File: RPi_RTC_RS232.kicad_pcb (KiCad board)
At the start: 2 copper layers, 65 x 56 mm, 5 parts, among them J2 RPi_GPIO

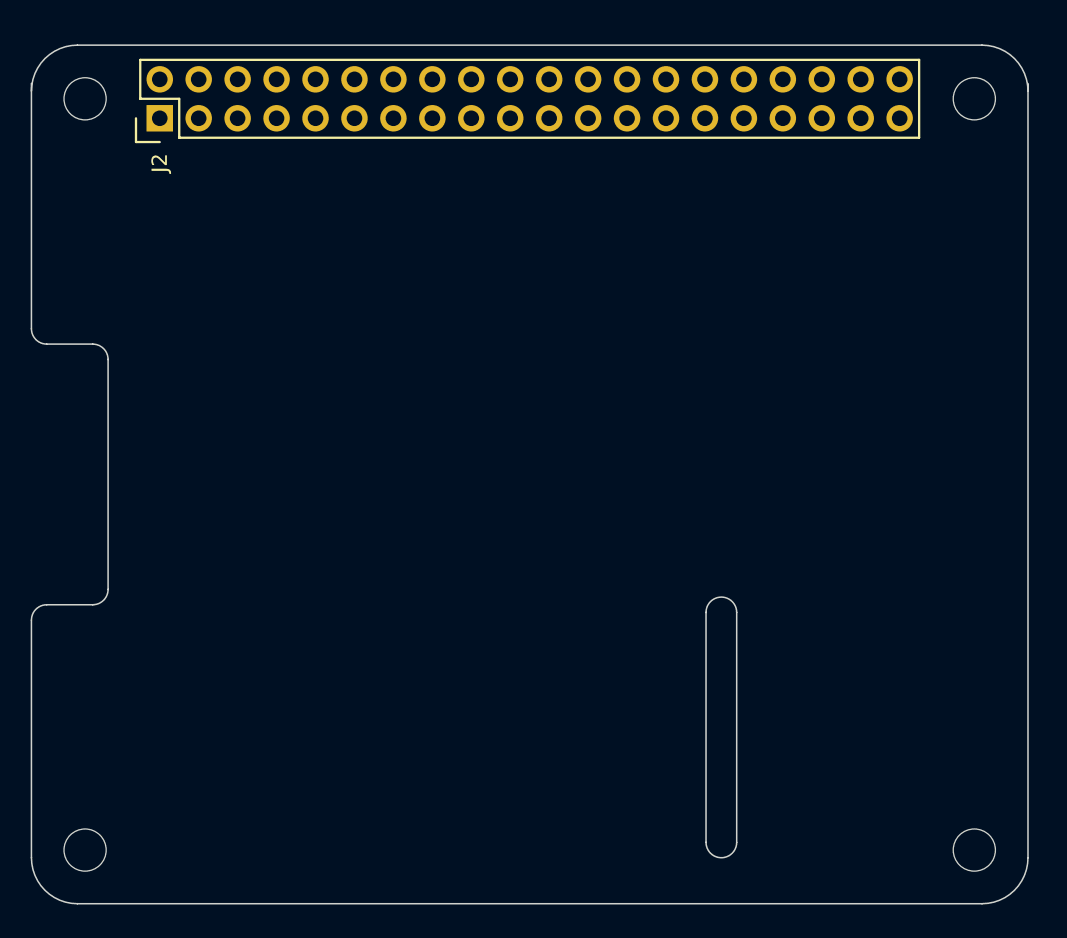
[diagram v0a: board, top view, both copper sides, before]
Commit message: schematic and provisional layout for RTC and RS232
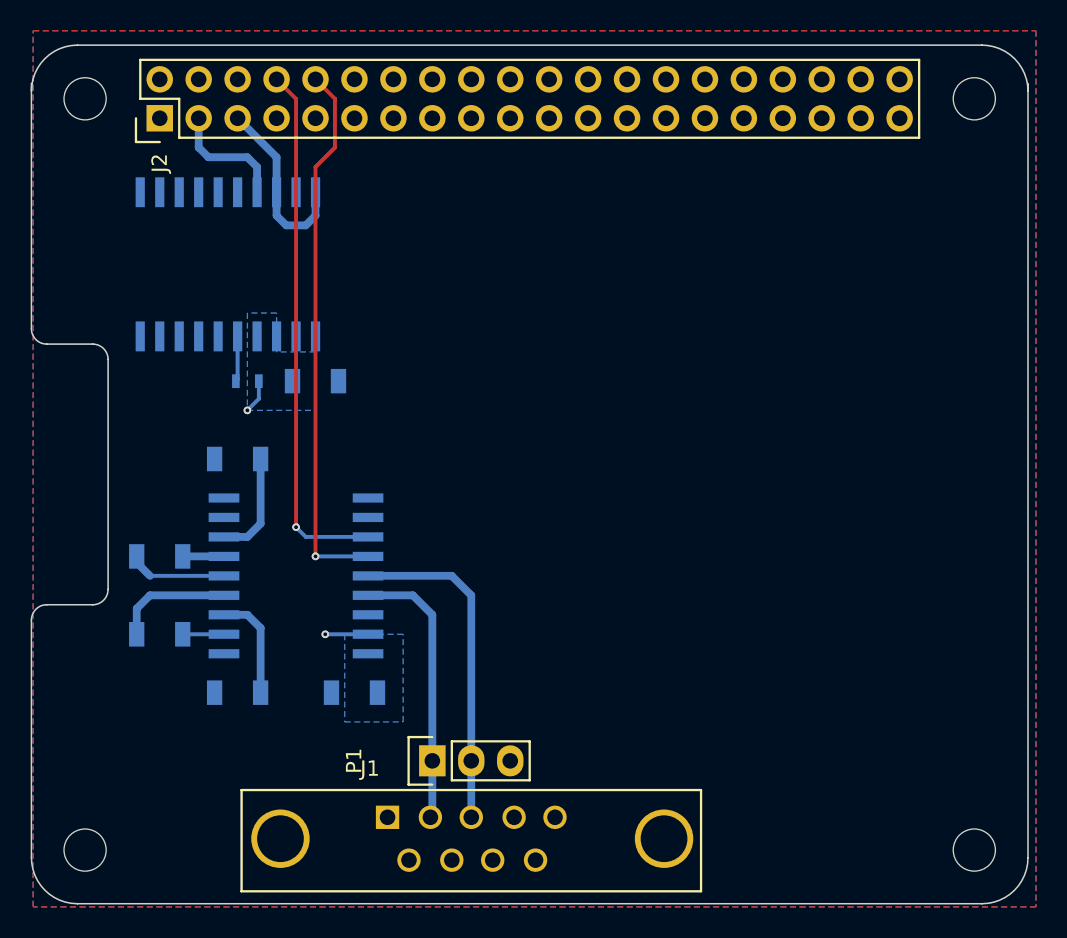
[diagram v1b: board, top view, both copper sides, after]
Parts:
- added C1: 1uF, Capacitors_SMD:C_1206, B.Cu at (121.9, 97.8)
- added C2: 0.1uF, Capacitors_SMD:C_1206, B.Cu at (124.5, 118.1)
- added C3: 0.1uF, Capacitors_SMD:C_1206, B.Cu at (111.8, 114.3)
- added C4: 0.1uF, Capacitors_SMD:C_1206, B.Cu at (111.8, 109.2)
- added C5: 0.1uF, Capacitors_SMD:C_1206, B.Cu at (116.8, 102.9)
- added C6: 0.1uF, Capacitors_SMD:C_1206, B.Cu at (116.8, 118.1)
- added IC1: MAX3222, Housings_SOIC:SOIC-18_7.5x11.6mm_Pitch1.27mm, B.Cu at (120.7, 110.5)
- added J1: DB9, Connect:DB9MD, F.Cu at (132.1, 127.6)
- added P1: CONN_01X03, Pin_Headers:Pin_Header_Straight_1x03, F.Cu at (129.5, 122.6)
- added R1: R, Resistors_SMD:R_0603, B.Cu at (117.5, 97.8)
- added U1: DS3232, Housings_SOIC:SOIC-20_7.5x12.8mm_Pitch1.27mm, B.Cu at (116.2, 90.2)
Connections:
- J2 pad 1: Net-(J2-Pad1) -> +3.3VP
- J2 pad 10: Net-(J2-Pad10) -> /RS232/RPi_R1
- J2 pad 14: Net-(J2-Pad14) -> GND
- J2 pad 17: Net-(J2-Pad17) -> +3.3VP
- J2 pad 2: Net-(J2-Pad2) -> +5VP
- J2 pad 20: Net-(J2-Pad20) -> GND
- J2 pad 25: Net-(J2-Pad25) -> GND
- J2 pad 3: Net-(J2-Pad3) -> /RPi_GPIO/SDA
- J2 pad 30: Net-(J2-Pad30) -> GND
- J2 pad 34: Net-(J2-Pad34) -> GND
- J2 pad 39: Net-(J2-Pad39) -> GND
- J2 pad 4: Net-(J2-Pad4) -> +5VP
- J2 pad 5: Net-(J2-Pad5) -> /RPi_GPIO/SCL
- J2 pad 6: Net-(J2-Pad6) -> GND
- J2 pad 8: Net-(J2-Pad8) -> /RS232/RPi_T1
- J2 pad 9: Net-(J2-Pad9) -> GND
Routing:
- net /RS232/RPi_R1: track 0.00 -> 35.6 mm, vias 0 -> 1
- net /RS232/RPi_T1: track 0.00 -> 34.7 mm, vias 0 -> 1
- net /RS232/RS232_R1: track 0.00 -> 21.7 mm
- net /RS232/RS232_T1: track 0.00 -> 18.0 mm
- net /RPi_GPIO/SCL: track 0.00 -> 12.0 mm
- net /RPi_GPIO/SDA: track 0.00 -> 7.89 mm
- net Net-(C3-Pad2): track 0.00 -> 7.72 mm
- net Net-(C6-Pad1): track 0.00 -> 6.96 mm
- net Net-(C5-Pad1): track 0.00 -> 6.96 mm
- net Net-(C4-Pad1): track 0.00 -> 6.45 mm
- net VCC: track 0.00 -> 5.01 mm, vias 0 -> 2
- net /RTC/SQW: track 0.00 -> 2.97 mm
- net Net-(C4-Pad2): track 0.00 -> 2.69 mm
- net Net-(C3-Pad1): track 0.00 -> 2.69 mm
- added copper zone on B.Cu, net GND
- added copper zone on B.Cu, net VCC
- added copper zone on F.Cu, net VCC
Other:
- outline, holes or cut-outs redrawn
- net class Default: clearance 0.2 -> 0.254; trace_width 0.25 -> 0.508; via_dia 0.6 -> 0.508
- net class Power added: clearance 0.508, trace_width 0.508, via_dia 0.508, via_drill 0.4
- net class Small added: clearance 0.254, trace_width 0.254, via_dia 0.508, via_drill 0.4
- rule trace_clearance: 0.2 -> 0.254
- rule trace_min: 0.01 -> 0.0254
- rule via_min_drill: 0.3 -> 0.254
- rule via_min_size: 0.4 -> 0.254
